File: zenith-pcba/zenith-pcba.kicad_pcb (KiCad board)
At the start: 2 copper layers, 2 parts, among them U1 XC7A50T-CSG325, U2 K4B4G1646E-BCNB

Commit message: feat(pcba): initial programmer setup
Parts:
- added J1: USB_C_Receptacle_USB2.0_16P, Connector_USB:USB_C_Receptacle_GCT_USB4105-xx-A_16P_TopMnt_Horizontal, F.Cu at (150.6, 58.3)
- added U3: CH347T, easyeda2kicad:TSSOP-20_L6.5-W4.4-P0.65-LS6.4-BL, F.Cu at (177.9, 77.2)
- moved U2 53.6 mm to (138.1, 60.5)
- moved U1 25.3 mm to (162.5, 82.0)
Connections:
- U1 pad A1: GND -> unconnected-(U1F-GND-PadA1)
- U1 pad A11: GND -> unconnected-(U1F-GND-PadA11)
- U1 pad A18: GND -> unconnected-(U1F-GND-PadA18)
- U1 pad A5: GND -> unconnected-(U1F-GND-PadA5)
- U1 pad A7: GND -> unconnected-(U1F-GND-PadA7)
- U1 pad A8: GND -> unconnected-(U1F-GND-PadA8)
- U1 pad B18: GND -> unconnected-(U1F-GND-PadB18)
- U1 pad B3: GND -> unconnected-(U1F-GND-PadB3)
- U1 pad B7: GND -> unconnected-(U1F-GND-PadB7)
- U1 pad B8: GND -> unconnected-(U1F-GND-PadB8)
- U1 pad C15: GND -> unconnected-(U1F-GND-PadC15)
- U1 pad C2: GND -> unconnected-(U1F-GND-PadC2)
- U1 pad C6: GND -> unconnected-(U1F-GND-PadC6)
- U1 pad C7: GND -> unconnected-(U1F-GND-PadC7)
- U1 pad D12: GND -> unconnected-(U1F-GND-PadD12)
- U1 pad D3: GND -> unconnected-(U1F-GND-PadD3)
- U1 pad D4: GND -> unconnected-(U1F-GND-PadD4)
- U1 pad D7: GND -> unconnected-(U1F-GND-PadD7)
- U1 pad E2: GND -> unconnected-(U1F-GND-PadE2)
- U1 pad E6: GND -> unconnected-(U1F-GND-PadE6)
- U1 pad E7: GND -> unconnected-(U1F-GND-PadE7)
- U1 pad E9: GND -> unconnected-(U1F-GND-PadE9)
- U1 pad F10: GND -> unconnected-(U1F-GND-PadF10)
- U1 pad F16: GND -> unconnected-(U1F-GND-PadF16)
- U1 pad F4: GND -> unconnected-(U1F-GND-PadF4)
- U1 pad F6: GND -> unconnected-(U1F-GND-PadF6)
- U1 pad F8: unconnected-(U1E-TCK_0-PadF8) -> Net-(U1E-TCK_0)
- U1 pad G1: GND -> unconnected-(U1F-GND-PadG1)
- U1 pad G11: GND -> unconnected-(U1F-GND-PadG11)
- U1 pad G13: GND -> unconnected-(U1F-GND-PadG13)
- U1 pad G5: GND -> unconnected-(U1F-GND-PadG5)
- U1 pad G6: GND -> unconnected-(U1F-GND-PadG6)
- U1 pad G7: GND -> unconnected-(U1F-GND-PadG7)
- U1 pad G9: GND -> unconnected-(U1F-GND-PadG9)
- U1 pad H10: GND -> unconnected-(U1F-GND-PadH10)
- U1 pad H12: GND -> unconnected-(U1F-GND-PadH12)
- U1 pad H3: GND -> unconnected-(U1F-GND-PadH3)
- U1 pad H4: GND -> unconnected-(U1F-GND-PadH4)
- U1 pad H5: GND -> unconnected-(U1F-GND-PadH5)
- U1 pad H6: GND -> unconnected-(U1F-GND-PadH6)
- U1 pad H8: GND -> unconnected-(U1F-GND-PadH8)
- U1 pad J1: GND -> unconnected-(U1F-GND-PadJ1)
- U1 pad J11: GND -> unconnected-(U1F-GND-PadJ11)
- U1 pad J13: GND -> unconnected-(U1F-GND-PadJ13)
- U1 pad J17: GND -> unconnected-(U1F-GND-PadJ17)
- U1 pad J2: GND -> unconnected-(U1F-GND-PadJ2)
- U1 pad J3: GND -> unconnected-(U1F-GND-PadJ3)
- U1 pad J7: GND -> unconnected-(U1F-GND-PadJ7)
- U1 pad J9: GND -> unconnected-(U1F-GNDADC_0-PadJ9)
- U1 pad K12: GND -> unconnected-(U1F-GND-PadK12)
- U1 pad K14: GND -> unconnected-(U1F-GND-PadK14)
- U1 pad K4: GND -> unconnected-(U1F-GND-PadK4)
- U1 pad K8: GND -> unconnected-(U1F-GND-PadK8)
- U1 pad L1: GND -> unconnected-(U1F-GND-PadL1)
- U1 pad L11: GND -> unconnected-(U1F-GND-PadL11)
- U1 pad L13: GND -> unconnected-(U1F-GND-PadL13)
- U1 pad L7: GND -> unconnected-(U1F-GND-PadL7)
- U1 pad M12: GND -> unconnected-(U1F-GND-PadM12)
- U1 pad M18: GND -> unconnected-(U1F-GND-PadM18)
- U1 pad M8: GND -> unconnected-(U1F-GND-PadM8)
- U1 pad N11: GND -> unconnected-(U1F-GND-PadN11)
- U1 pad N13: GND -> unconnected-(U1F-GND-PadN13)
- U1 pad N15: GND -> unconnected-(U1F-GND-PadN15)
- U1 pad N5: GND -> unconnected-(U1F-GND-PadN5)
- U1 pad N7: GND -> unconnected-(U1F-GND-PadN7)
- U1 pad N9: GND -> unconnected-(U1F-GND-PadN9)
- U1 pad P12: GND -> unconnected-(U1F-GND-PadP12)
- U1 pad P2: GND -> unconnected-(U1F-GND-PadP2)
- U1 pad P8: GND -> unconnected-(U1F-GND-PadP8)
- U1 pad R8: unconnected-(U1E-TMS_0-PadR8) -> Net-(U1E-TMS_0)
- U1 pad R9: GND -> unconnected-(U1F-GND-PadR9)
- U1 pad T16: GND -> unconnected-(U1F-GND-PadT16)
- U1 pad T6: GND -> unconnected-(U1F-GND-PadT6)
- U1 pad T8: unconnected-(U1E-TDO_0-PadT8) -> Net-(U1E-TDO_0)
- U1 pad T9: unconnected-(U1E-TDI_0-PadT9) -> Net-(U1E-TDI_0)
- U1 pad U13: GND -> unconnected-(U1F-GND-PadU13)
- U1 pad U3: GND -> unconnected-(U1F-GND-PadU3)
- U1 pad V1: GND -> unconnected-(U1F-GND-PadV1)
- U1 pad V10: GND -> unconnected-(U1F-GND-PadV10)
- U1 pad V18: GND -> unconnected-(U1F-GND-PadV18)
- U2 pad A9: /Root/GND -> unconnected-(U2-VSS-PadA9)
- U2 pad T1: /Root/GND -> unconnected-(U2-VSS-PadT1)
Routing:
- net GND: track 15.1 -> 0.00 mm, vias 72 -> 0
- net unconnected-(U1B-IO_L3N_T0_DQS_34-PadK1): track 0.44 -> 0.00 mm, vias 1 -> 0
- net unconnected-(U1C-MGTPRXP0_216-PadE4): track 0.15 -> 0.00 mm, vias 1 -> 0
- added copper zone on B.Cu, net (none)
- removed copper zone on B.Cu, net GND

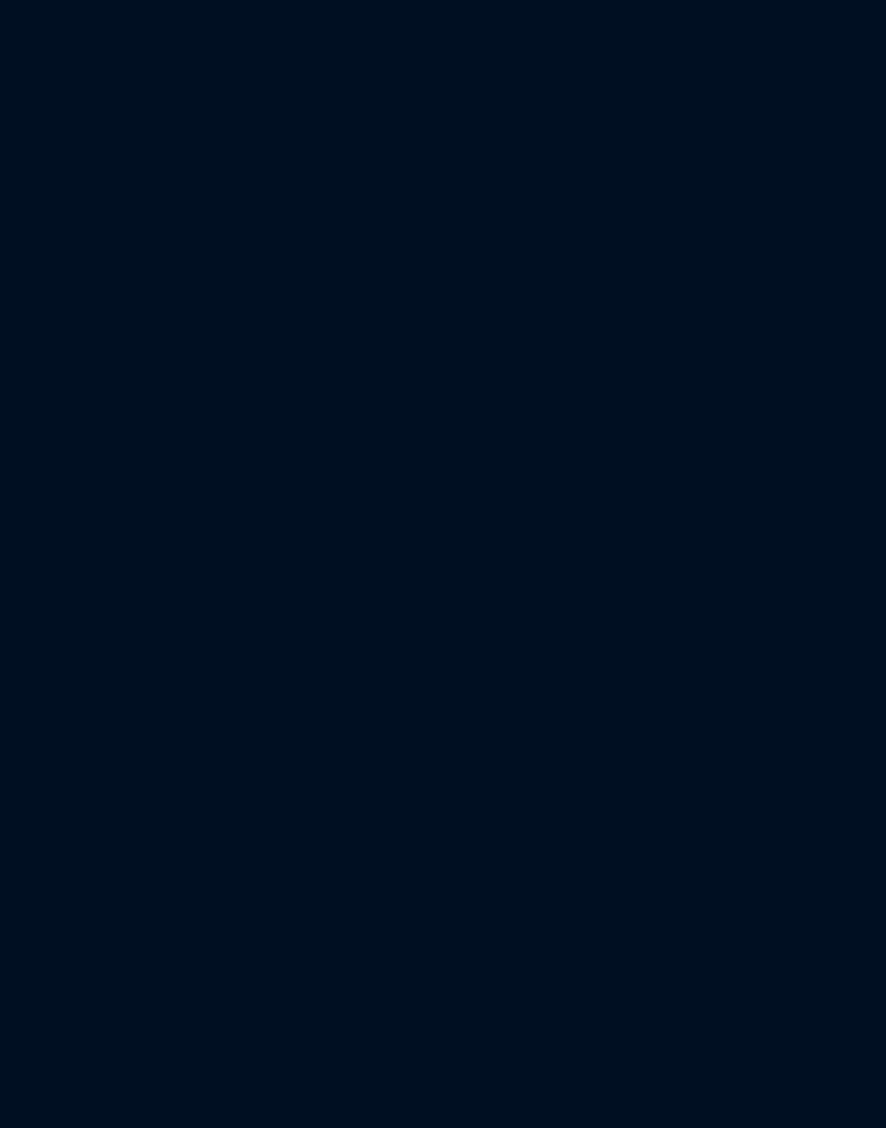
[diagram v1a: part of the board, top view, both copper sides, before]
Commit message: feat(pcba): programmer connections and uart
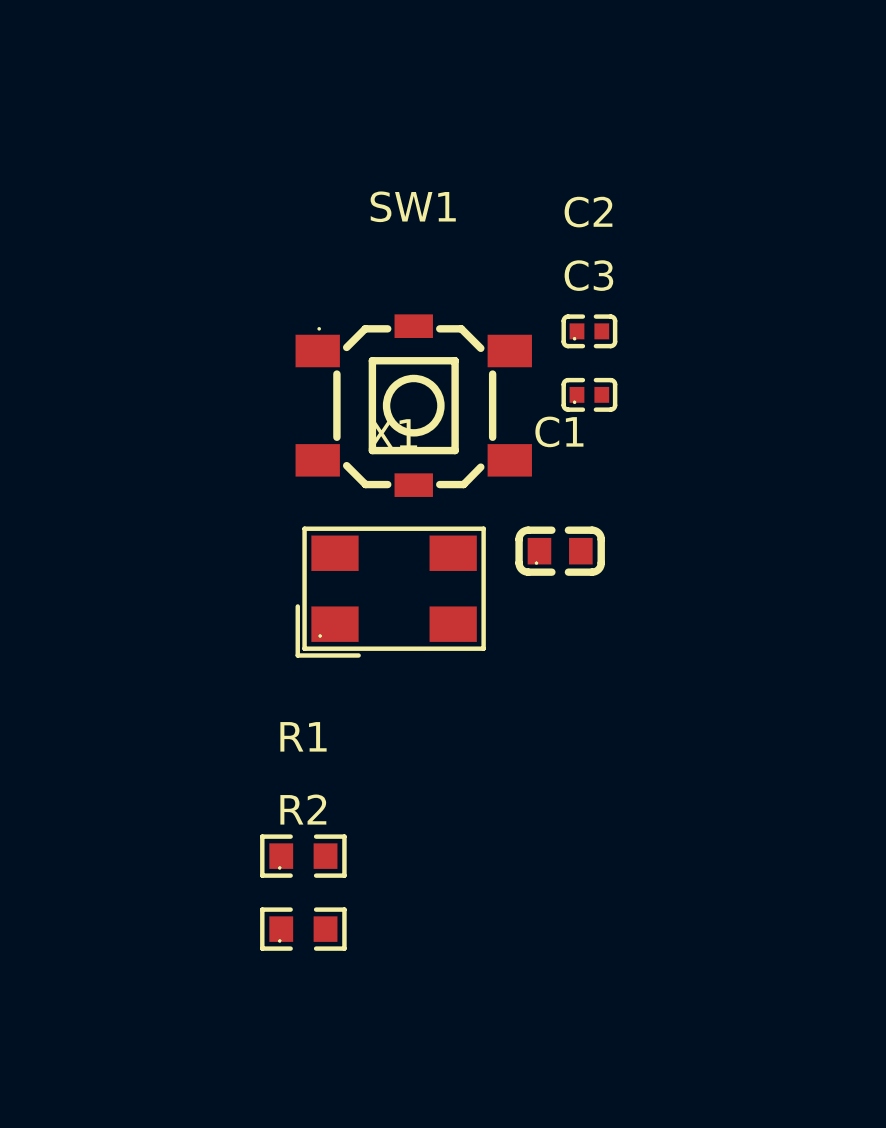
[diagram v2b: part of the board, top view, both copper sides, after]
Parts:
- added C1: CL10B104KA8NNNC, easyeda2kicad:C0603, F.Cu at (212.4, 73.0)
- added C2: 0402CG220J500NT, easyeda2kicad:C0402, F.Cu at (213.3, 65.6)
- added C3: 0402CG220J500NT, easyeda2kicad:C0402, F.Cu at (213.3, 67.7)
- added R1: RC0603FR-074K7L, easyeda2kicad:R0603, F.Cu at (203.7, 83.3)
- added R2: RC0603FR-074K7L, easyeda2kicad:R0603, F.Cu at (203.7, 85.8)
- added SW1: G4R152312, easyeda2kicad:SW-SMD_4P-L5.2-W5.2-P3.70-LS6.4_UK-B0233XX, F.Cu at (207.4, 68.1)
- added X1: SX5B8.000F1520F30, easyeda2kicad:CYSTAL-SMD_4P-L5.0-W3.2-BL, F.Cu at (206.7, 74.3)
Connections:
- U1 pad K5: unconnected-(U1B-IO_L1N_T0_34-PadK5) -> UARTTX
- U1 pad K6: unconnected-(U1B-IO_L1P_T0_34-PadK6) -> UARTRX
- U3 pad 1: unconnected-(U3-~{RST}-Pad1) -> Net-(U3-~{RST})
- U3 pad 10: unconnected-(U3-TNOW1/DTR1-Pad10) -> Net-(U3-TNOW1/DTR1)
- U3 pad 13: unconnected-(U3-RTS1/GPIO7-Pad13) -> Net-(U3-RTS1/GPIO7)
- U3 pad 19: unconnected-(U3-XI-Pad19) -> Net-(U3-XI)
- U3 pad 20: unconnected-(U3-XO-Pad20) -> Net-(U3-XO)
- U3 pad 3: unconnected-(U3-TXD1-Pad3) -> UARTRX
- U3 pad 4: unconnected-(U3-RXD1-Pad4) -> UARTTX

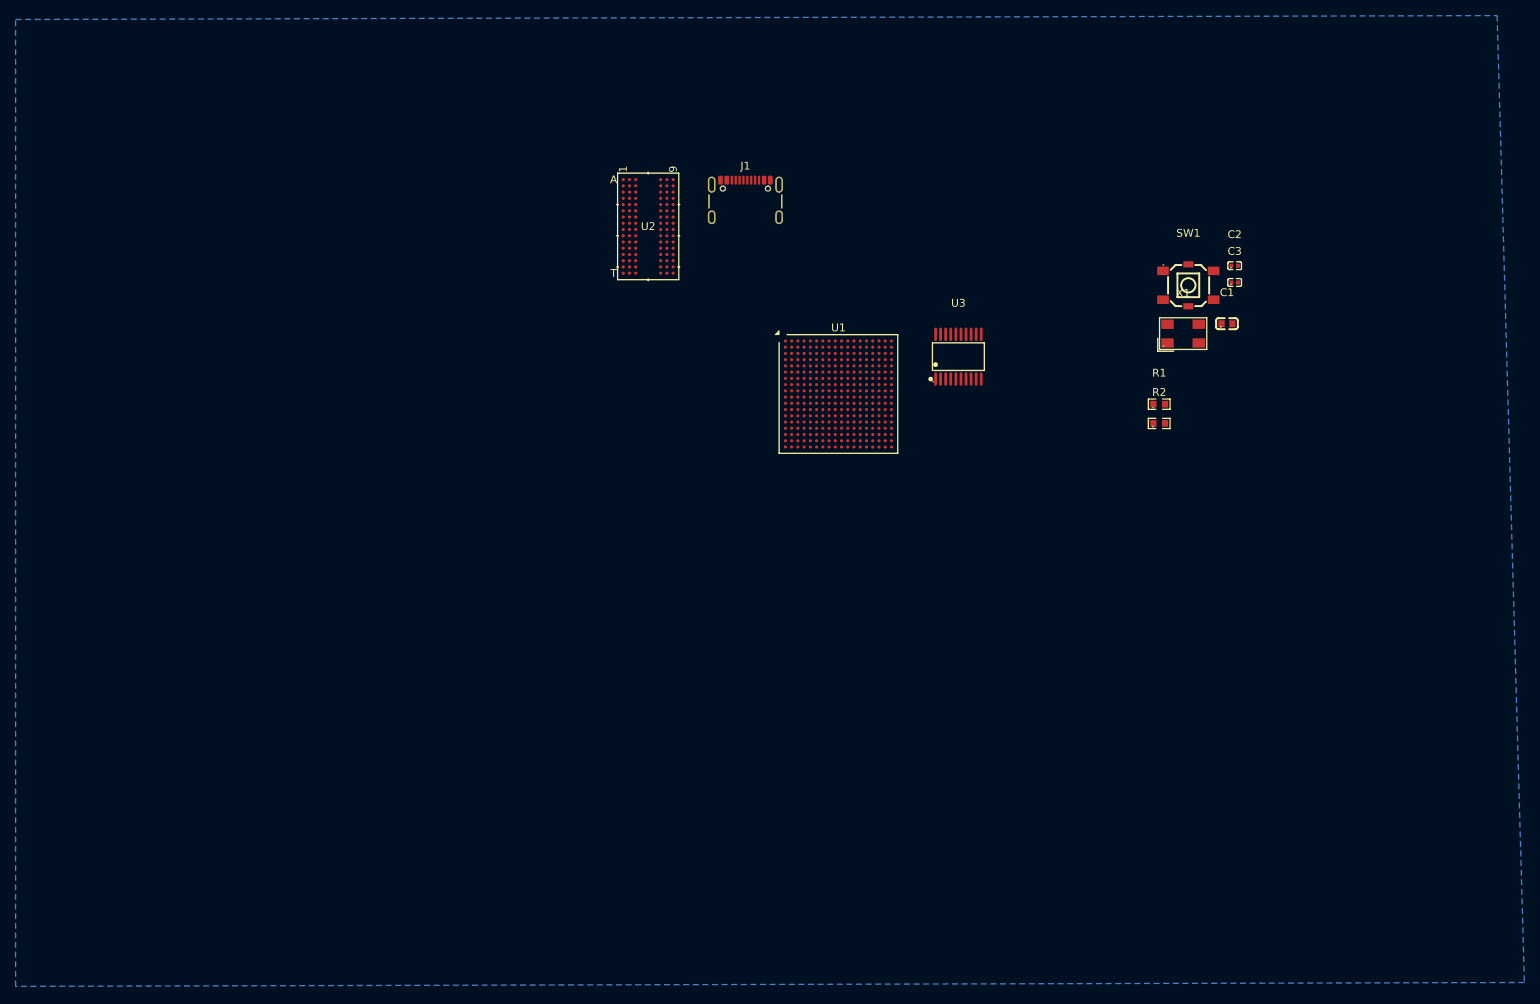
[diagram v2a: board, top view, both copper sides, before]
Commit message: fix(pcba): 3d models
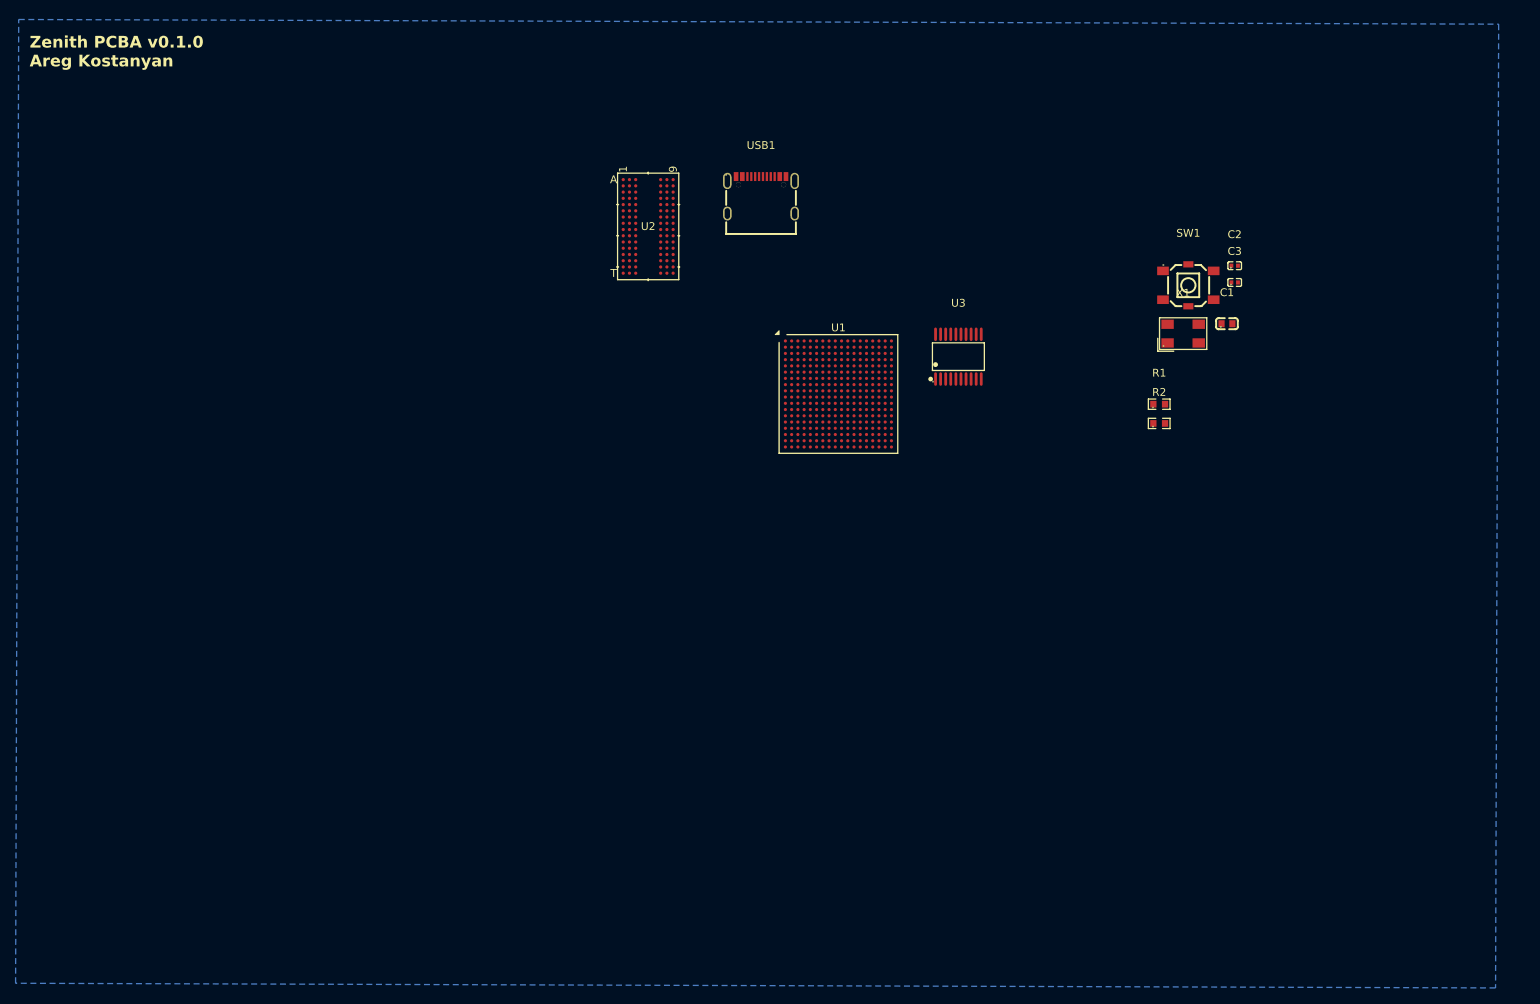
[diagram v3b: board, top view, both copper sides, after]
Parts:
- removed J1: USB_C_Receptacle_USB2.0_16P, Connector_USB:USB_C_Receptacle_GCT_USB4105-xx-A_16P_TopMnt_Horizontal
- added USB1: USB4105-GF-A, easyeda2kicad:TYPE-C-SMD_SBC-160S1A-20-S412, F.Cu at (152.6, 56.5)
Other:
- board text added: "Zenith PCBA v0.1.0 Areg Kostanyan"
